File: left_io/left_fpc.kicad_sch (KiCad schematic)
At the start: 1 part

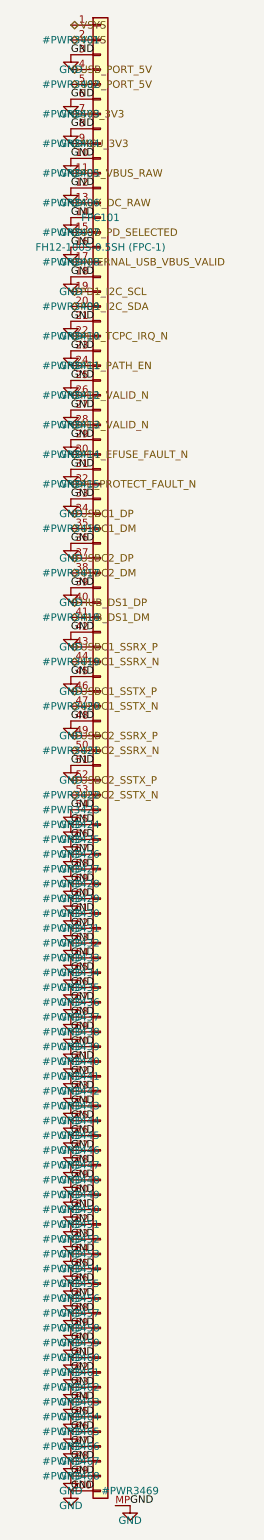
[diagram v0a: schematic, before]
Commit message: Phase 4 deep audit: FH41-68S connectors, placement hygiene, one-shot fixes
Found and fixed four board-killers in the pre-fab audit:

1. Fictional connector: the Hirose FH12 series stops at 60 positions, so
   the 100-pin FH12-100S used for FPC-1/FPC-2 does not exist.  Replaced
   with the FH41-68S-0.5SH(05) (shielded-FFC, 68 positions; FPC-1 uses
   pins 1-53, FPC-2 pins 1-61):
   - new footprint derived from KiCad's FH41-30S (68 signal pads, MP at
     +/-18, 14 SH solder-holds, 38mm body) with SH pads tied to GND
   - new 68-pin symbol (Conn_01x68_FFC_MP), pin maps trimmed to 68
   - fictional FH12-100S footprint/symbol/script removed
   - cable spec updated (68-pin shielded FFC, one type for both)

2. Connector courtyard conflicts: parts sat under connector bodies
   (pads cleared, bodies collided).  Placement now enforces courtyard
   clearance against the connector body; the resolver scans with
   courtyard checks; a double-shift bug that hid re-placed parts' true
   positions was fixed.

3. FPC-3 orientation: the FH12's FPC enters from the +y side; both FPC-3
   connectors faced away from the seam.  FPC105 -> (123.5, 6.5) rot 180,
   FPC106 -> (30, 54) rot 0 so the cable exits the center bottom edge
   and enters the BMS top edge.

4. Original-layout defects: 16 genuine pad-pad shorts (inductor pads
   swallowing caps, passives on each other, parts on mounting holes) and
   23 parts inside the hinge cutouts (physically off the board) are all
   moved to legal spots; zones refilled against the final placement.

New post-build hygiene sweep (fix_board_hygiene.py) uses the final board
text as the geometry oracle, converges to a clean state, and reports
residuals instead of dropping them.

Final DRC: 0 shorts / 0 clearance / 0 hole violations on all four boards
(bms fully clean).  Remaining: courtyard touches around the Mu socket and
M.2 slot (design-inherent moat), chassis-edge copper, zone islands, silk
cosmetics, and unrouted nets (Phase 4b).  Gate: SCHEMATIC R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
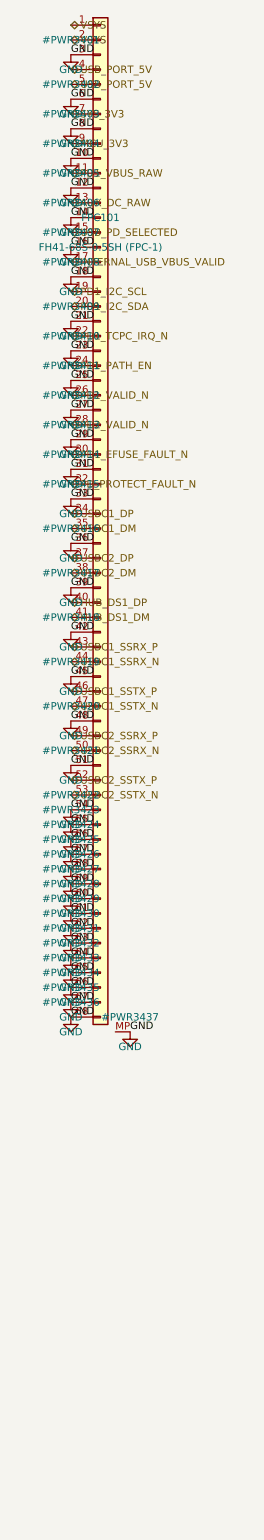
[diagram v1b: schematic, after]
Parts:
- FPC101: value FH12-100S-0.5SH (FPC-1) -> FH41-68S-0.5SH (FPC-1); footprint ducktop2:FH12-100S-0.5SH_1x100-1MP_P0.50mm_Horizontal -> ducktop2:Hirose_FH41-68S-0.5SH_1x68_1MP_1SH_P0.5mm_Horizontal; symbol Conn_01x100_FFC_MP:Conn_01x100_FFC_MP -> Conn_01x68_FFC_MP:Conn_01x68_FFC_MP
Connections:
- net GND: no longer FPC101.100 (Pin_100), FPC101.69 (Pin_69), FPC101.70 (Pin_70), FPC101.71 (Pin_71), FPC101.72 (Pin_72), FPC101.73 (Pin_73), FPC101.74 (Pin_74), FPC101.75 (Pin_75), FPC101.76 (Pin_76), FPC101.77 (Pin_77), FPC101.78 (Pin_78), FPC101.79 (Pin_79), FPC101.80 (Pin_80), FPC101.81 (Pin_81), FPC101.82 (Pin_82), FPC101.83 (Pin_83), FPC101.84 (Pin_84), FPC101.85 (Pin_85), FPC101.86 (Pin_86), FPC101.87 (Pin_87), FPC101.88 (Pin_88), FPC101.89 (Pin_89), FPC101.90 (Pin_90), FPC101.91 (Pin_91), FPC101.92 (Pin_92), FPC101.93 (Pin_93), FPC101.94 (Pin_94), FPC101.95 (Pin_95), FPC101.96 (Pin_96), FPC101.97 (Pin_97), FPC101.98 (Pin_98), FPC101.99 (Pin_99)

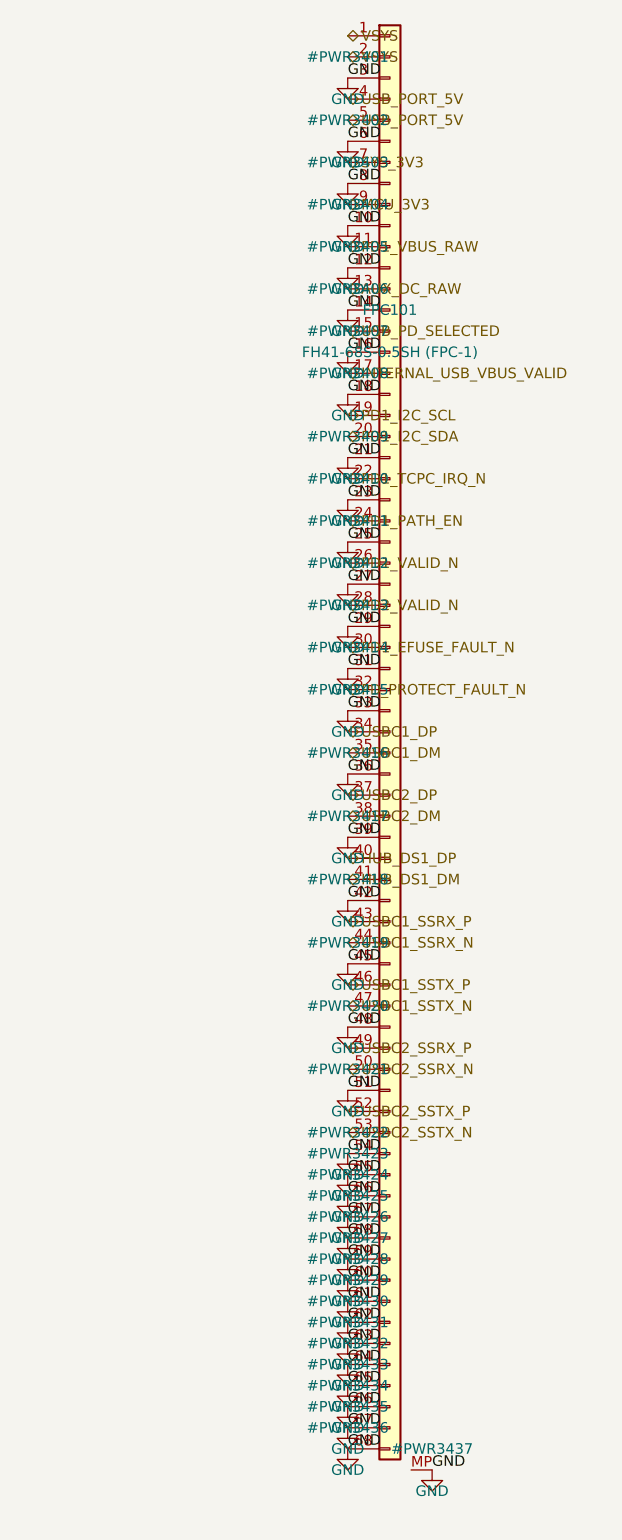
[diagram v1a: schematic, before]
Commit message: Phase 5: second-opinion audit remediation + rebuilt, verified board pipeline
Second-opinion AI audit found A-tier defects; remediation applied and the
board pipeline rebuilt on a known-good base with the fixes it needed:

- electrical: LTC4418IUF symbol pinout corrected (both selectors were
  dead as drawn); center charge cascade (U15 <- U15B, PD1 > PD2 > AUX);
  pack negative never crosses FPC-3, 15-pin FG_VSS return; power-budgeted
  FPC pin maps (0.4 A/pin derate); J12/DS4 completed; AUX source fuse
- FH41-68S footprint: 13 datasheet-correct SH pads + SH pin in symbol
- connector geometry settled against the Hirose FH12 2D drawing: FFC
  enters opposite the solder pins (mouth = local +Y); reversed side-B
  maps are correct for the 180-deg-mounted pairs; rotations set so mouths
  face across every seam
- pipeline (generate_split_boards.py): per-pin pad-net resync from the
  netlists (kills shadow nets for good), netlist-exact name
  normalization, netlist-only part injection (cascade, probe headers),
  zone refill after outline swap, read-before-write race fixed, orphan
  parts dropped loudly, non-zero exit on unresolved overlaps
- monolith board relocated to old/monolith_ducktop2.kicad_pcb (placement
  oracle for the center cut only)

verified end state: 4 boards 0 shorts / 0 clearance / 0 drill, 0 boundary
crossings, 6/6 connectors contract-exact with mouths facing, 0 shadow
nets, gates PASS x4, ERC 0 x4. routing next (499 nets/board).
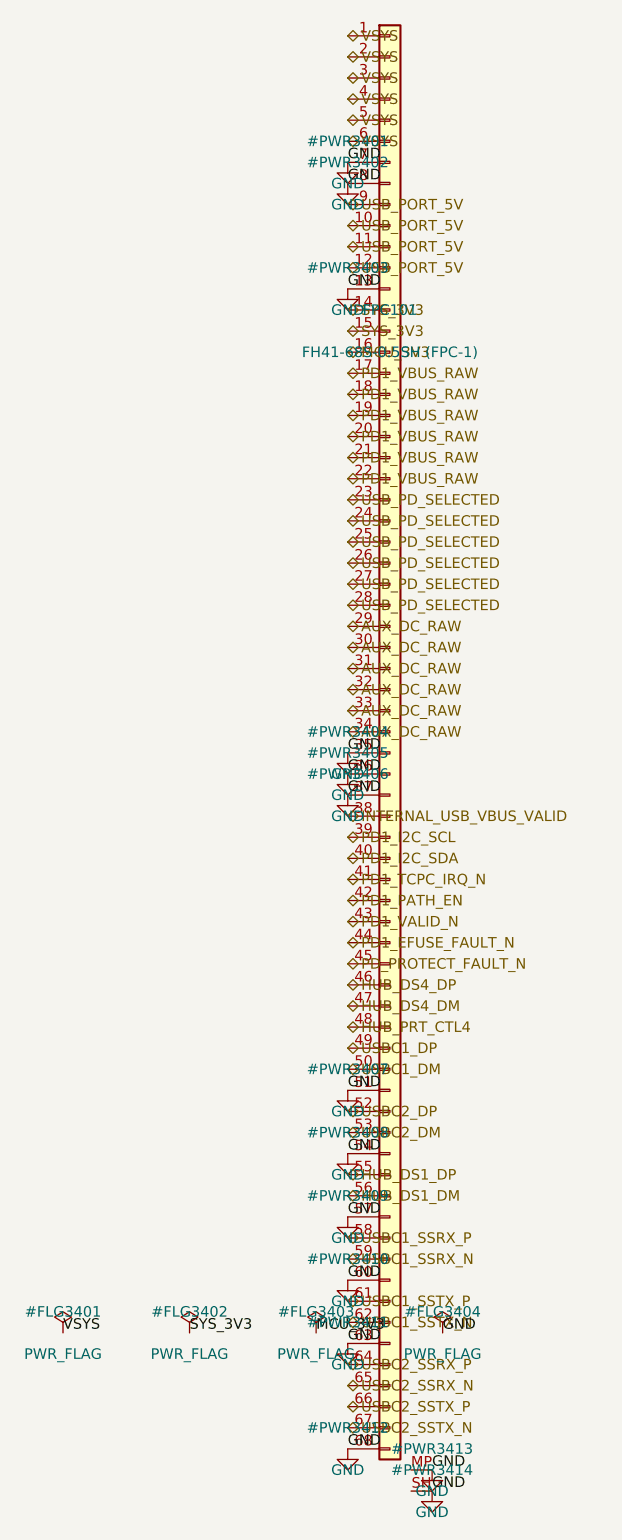
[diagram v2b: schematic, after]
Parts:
- FPC101: MPN (none) -> FH41-68S-0.5SH(05); Manufacturer (none) -> Hirose
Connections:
- net PD2_VALID_N is gone; now on net USB_PD_SELECTED: FPC101.28 (Pin_28)
- net AUX_DC_RAW: now also FPC101.29 (Pin_29), FPC101.30 (Pin_30), FPC101.31 (Pin_31), FPC101.32 (Pin_32), FPC101.33 (Pin_33), FPC101.34 (Pin_34); no longer FPC101.13 (Pin_13)
- net GND: now also FPC101.13 (Pin_13), FPC101.35 (Pin_35), FPC101.37 (Pin_37), FPC101.7 (Pin_7), FPC101.SH; no longer FPC101.10 (Pin_10), FPC101.12 (Pin_12), FPC101.14 (Pin_14), FPC101.16 (Pin_16), FPC101.18 (Pin_18), FPC101.21 (Pin_21), FPC101.23 (Pin_23), FPC101.25 (Pin_25), FPC101.27 (Pin_27), FPC101.29 (Pin_29), FPC101.3 (Pin_3), FPC101.31 (Pin_31), FPC101.33 (Pin_33), FPC101.39 (Pin_39), FPC101.42 (Pin_42), FPC101.45 (Pin_45), FPC101.48 (Pin_48), FPC101.55 (Pin_55), FPC101.56 (Pin_56), FPC101.58 (Pin_58), FPC101.59 (Pin_59), FPC101.6 (Pin_6), FPC101.61 (Pin_61), FPC101.62 (Pin_62), FPC101.64 (Pin_64), FPC101.65 (Pin_65), FPC101.66 (Pin_66), FPC101.67 (Pin_67)
- net HUB_DS1_DM: now also FPC101.56 (Pin_56); no longer FPC101.41 (Pin_41)
- net HUB_DS1_DP: now also FPC101.55 (Pin_55); no longer FPC101.40 (Pin_40)
- net INTERNAL_USB_VBUS_VALID: now also FPC101.38 (Pin_38); no longer FPC101.17 (Pin_17)
- net MCU_3V3: now also FPC101.16 (Pin_16); no longer FPC101.9 (Pin_9)
- net PD1_EFUSE_FAULT_N: now also FPC101.44 (Pin_44); no longer FPC101.30 (Pin_30)
- net PD1_I2C_SCL: now also FPC101.39 (Pin_39); no longer FPC101.19 (Pin_19)
- net PD1_I2C_SDA: now also FPC101.40 (Pin_40); no longer FPC101.20 (Pin_20)
- net PD1_PATH_EN: now also FPC101.42 (Pin_42); no longer FPC101.24 (Pin_24)
- net PD1_TCPC_IRQ_N: now also FPC101.41 (Pin_41); no longer FPC101.22 (Pin_22)
- net PD1_VALID_N: now also FPC101.43 (Pin_43); no longer FPC101.26 (Pin_26)
- net PD1_VBUS_RAW: now also FPC101.17 (Pin_17), FPC101.18 (Pin_18), FPC101.19 (Pin_19), FPC101.20 (Pin_20), FPC101.21 (Pin_21), FPC101.22 (Pin_22); no longer FPC101.11 (Pin_11)
- net PD_PROTECT_FAULT_N: now also FPC101.45 (Pin_45); no longer FPC101.32 (Pin_32)
- net SYS_3V3: now also FPC101.14 (Pin_14), FPC101.15 (Pin_15); no longer FPC101.7 (Pin_7)
- net USBC1_DM: now also FPC101.50 (Pin_50); no longer FPC101.35 (Pin_35)
- net USBC1_DP: now also FPC101.49 (Pin_49); no longer FPC101.34 (Pin_34)
- net USBC1_SSRX_N: now also FPC101.59 (Pin_59); no longer FPC101.44 (Pin_44)
- net USBC1_SSRX_P: now also FPC101.58 (Pin_58); no longer FPC101.43 (Pin_43)
- net USBC1_SSTX_N: now also FPC101.62 (Pin_62); no longer FPC101.47 (Pin_47)
- net USBC1_SSTX_P: now also FPC101.61 (Pin_61); no longer FPC101.46 (Pin_46)
- net USBC2_DM: now also FPC101.53 (Pin_53); no longer FPC101.38 (Pin_38)
- net USBC2_DP: now also FPC101.52 (Pin_52); no longer FPC101.37 (Pin_37)
- net USBC2_SSRX_N: now also FPC101.65 (Pin_65); no longer FPC101.50 (Pin_50)
- net USBC2_SSRX_P: now also FPC101.64 (Pin_64); no longer FPC101.49 (Pin_49)
- net USBC2_SSTX_N: now also FPC101.67 (Pin_67); no longer FPC101.53 (Pin_53)
- net USBC2_SSTX_P: now also FPC101.66 (Pin_66); no longer FPC101.52 (Pin_52)
- net USB_PD_SELECTED: now also FPC101.23 (Pin_23), FPC101.24 (Pin_24), FPC101.25 (Pin_25), FPC101.26 (Pin_26), FPC101.27 (Pin_27); no longer FPC101.15 (Pin_15)
- net USB_PORT_5V: now also FPC101.10 (Pin_10), FPC101.11 (Pin_11), FPC101.12 (Pin_12), FPC101.9 (Pin_9); no longer FPC101.4 (Pin_4), FPC101.5 (Pin_5)
- net VSYS: now also FPC101.3 (Pin_3), FPC101.4 (Pin_4), FPC101.5 (Pin_5), FPC101.6 (Pin_6)
- new net HUB_DS4_DM: FPC101.47 (Pin_47)
- new net HUB_DS4_DP: FPC101.46 (Pin_46)
- new net HUB_PRT_CTL4: FPC101.48 (Pin_48)

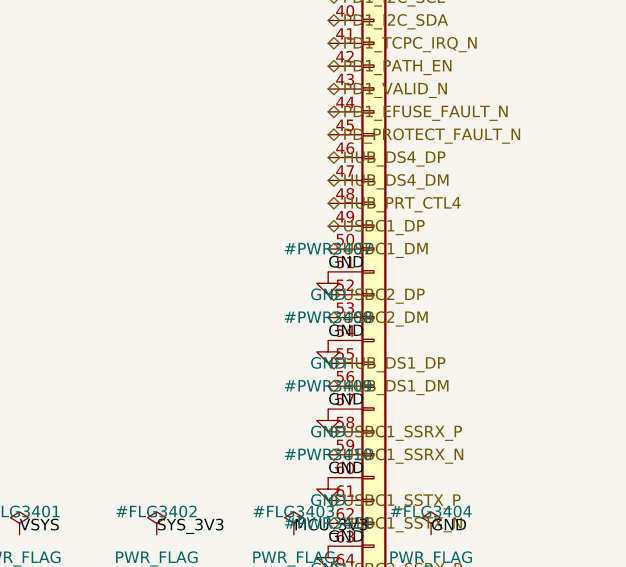
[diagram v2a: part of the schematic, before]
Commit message: get the main boards ready for routing
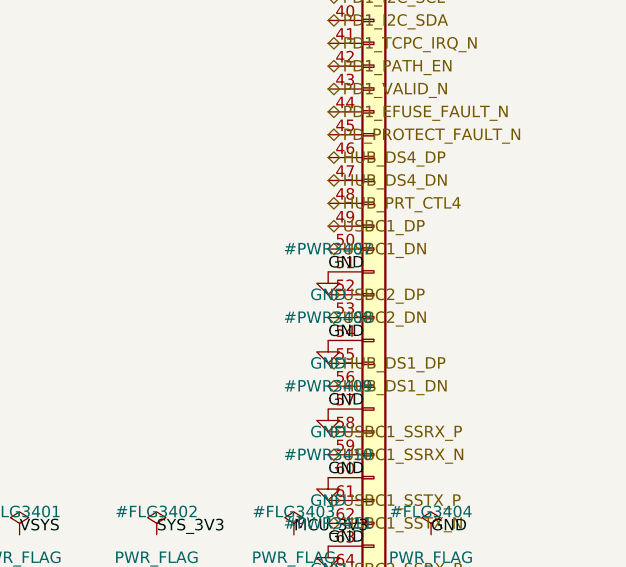
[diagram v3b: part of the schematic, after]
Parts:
- FPC101: MPN FH41-68S-0.5SH(05) -> FH41-68S-0.5SH(28)
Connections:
- net HUB_DS1_DM renamed HUB_DS1_DN
- net HUB_DS4_DM renamed HUB_DS4_DN
- net USBC1_DM renamed USBC1_DN
- net USBC2_DM renamed USBC2_DN
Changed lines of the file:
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@@
   (property "Datasheet" "" (at 59.69 299.72 0) (effects (font (size 1.27 1.27)) (hide yes)))
   (property "Manufacturer" "Hirose" (at 59.69 299.72 0) (effects (font (size 1.27 1.27)) (hide yes)))
-  (property "MPN" "FH41-68S-0.5SH(05)" (at 59.69 299.72 0) (effects (font (size 1.27 1.27)) (hide yes)))
+  (property "MPN" "FH41-68S-0.5SH(28)" (at 59.69 299.72 0) (effects (font (size 1.27 1.27)) (hide yes)))
   (pin "1")
   (pin "2")
@@
   (effects (font (size 1.27 1.27)) (justify left bottom))
 )
-(hierarchical_label "HUB_DS4_DM"
+(hierarchical_label "HUB_DS4_DN"
   (shape bidirectional)
   (at 54.61 381 0)
@@
   (effects (font (size 1.27 1.27)) (justify left bottom))
 )
-(hierarchical_label "USBC1_DM"
+(hierarchical_label "USBC1_DN"
   (shape bidirectional)
   (at 54.61 388.62 0)
@@
   (effects (font (size 1.27 1.27)) (justify left bottom))
 )
-(hierarchical_label "USBC2_DM"
+(hierarchical_label "USBC2_DN"
   (shape bidirectional)
   (at 54.61 396.24 0)
@@
   (effects (font (size 1.27 1.27)) (justify left bottom))
 )
-(hierarchical_label "HUB_DS1_DM"
+(hierarchical_label "HUB_DS1_DN"
   (shape bidirectional)
   (at 54.61 403.86 0)

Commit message: fix more power stuff and update the left board
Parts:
- added J2431: left power loom, straight-numbered, Connector_Molex:Molex_Micro-Fit_3.0_43045-1212_2x06_P3.00mm_Vertical, symbol Connector_Generic:Conn_02x06_Odd_Even
- added J2434: USB5 direct power loom, ducktop2:AMASS_XT30PW-F30_G_Y, symbol Connector_Generic:Conn_01x02
- added J2440, J2442: main ground strap, Connector_Wire:SolderWirePad_1x01_SMD_5x10mm, symbol Connector:TestPoint
- added R2440, R2441: 0.33, Resistor_SMD:R_0603_1608Metric, symbol Device:R
- FPC101: value FH41-68S-0.5SH (FPC-1) -> Molex5039084120 signal cable; footprint ducktop2:Hirose_FH41-68S-0.5SH_1x68_1MP_1SH_P0.5mm_Horizontal -> ducktop2:Molex_5039084120_1x41_P0.50mm_Horizontal; symbol Conn_01x68_FFC_MP:Conn_01x68_FFC_MP -> Conn_01x41_Signal_SH:Conn_01x41_Signal_SH; MPN FH41-68S-0.5SH(28) -> 5039084120; Manufacturer Hirose -> Molex
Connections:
- net AUX_DC_RAW: now also J2431.4 (Pin_4); no longer FPC101.29 (Pin_29), FPC101.30 (Pin_30), FPC101.31 (Pin_31), FPC101.32 (Pin_32), FPC101.33 (Pin_33), FPC101.34 (Pin_34)
- net GND: now also FPC101.1, FPC101.10, FPC101.16, FPC101.19, FPC101.22, FPC101.25, FPC101.29, FPC101.33, FPC101.4, J2431.10 (Pin_10), J2431.11 (Pin_11), J2431.12 (Pin_12), J2431.7 (Pin_7), J2431.8 (Pin_8), J2431.9 (Pin_9), J2434.1 (Pin_1), J2440.1, J2442.1, R2440.2, R2441.2; no longer FPC101.35 (Pin_35), FPC101.36 (Pin_36), FPC101.51 (Pin_51), FPC101.54 (Pin_54), FPC101.57 (Pin_57), FPC101.60 (Pin_60), FPC101.63 (Pin_63), FPC101.68 (Pin_68), FPC101.8 (Pin_8), FPC101.MP, FPC101.SH
- net HUB_DS1_DN: now also FPC101.21; no longer FPC101.56 (Pin_56)
- net HUB_DS1_DP: now also FPC101.20; no longer FPC101.55 (Pin_55)
- net HUB_DS4_DN: now also FPC101.24; no longer FPC101.47 (Pin_47)
- net HUB_DS4_DP: now also FPC101.23; no longer FPC101.46 (Pin_46)
- net HUB_PRT_CTL4: now also FPC101.40; no longer FPC101.48 (Pin_48)
- net INTERNAL_USB_VBUS_VALID: now also FPC101.41; no longer FPC101.38 (Pin_38)
- net MCU_3V3: now also J2431.6 (Pin_6); no longer FPC101.16 (Pin_16)
- net PD1_EFUSE_FAULT_N: now also FPC101.32; no longer FPC101.44 (Pin_44)
- net PD1_I2C_SCL: now also FPC101.26; no longer FPC101.39 (Pin_39)
- net PD1_I2C_SDA: now also FPC101.27; no longer FPC101.40 (Pin_40)
- net PD1_PATH_EN: now also FPC101.30; no longer FPC101.42 (Pin_42)
- net PD1_TCPC_IRQ_N: now also FPC101.28; no longer FPC101.41 (Pin_41)
- net PD1_VALID_N: now also FPC101.31; no longer FPC101.43 (Pin_43)
- net PD1_VBUS_RAW: now also J2431.2 (Pin_2); no longer FPC101.17 (Pin_17), FPC101.18 (Pin_18), FPC101.19 (Pin_19), FPC101.20 (Pin_20), FPC101.21 (Pin_21), FPC101.22 (Pin_22)
- net PD_PROTECT_FAULT_N: now also FPC101.34; no longer FPC101.45 (Pin_45)
- net SYS_3V3: now also J2431.5 (Pin_5); no longer FPC101.14 (Pin_14), FPC101.15 (Pin_15)
- net USBC1_DN: now also FPC101.15; no longer FPC101.50 (Pin_50)
- net USBC1_DP: now also FPC101.14; no longer FPC101.49 (Pin_49)
- net USBC1_SSRX_N: now also FPC101.3; no longer FPC101.59 (Pin_59)
- net USBC1_SSRX_P: now also FPC101.2; no longer FPC101.58 (Pin_58)
- net USBC1_SSTX_N: now also FPC101.6; no longer FPC101.62 (Pin_62)
- net USBC1_SSTX_P: now also FPC101.5; no longer FPC101.61 (Pin_61)
- net USBC2_DN: now also FPC101.18; no longer FPC101.53 (Pin_53)
- net USBC2_DP: now also FPC101.17; no longer FPC101.52 (Pin_52)
- net USBC2_SSRX_N: now also FPC101.9; no longer FPC101.65 (Pin_65)
- net USBC2_SSRX_P: now also FPC101.8; no longer FPC101.64 (Pin_64)
- net USBC2_SSTX_N: now also FPC101.12; no longer FPC101.67 (Pin_67)
- net USBC2_SSTX_P: now also FPC101.11; no longer FPC101.66 (Pin_66)
- net USB_PD_SELECTED: now also J2431.3 (Pin_3); no longer FPC101.23 (Pin_23), FPC101.24 (Pin_24), FPC101.25 (Pin_25), FPC101.26 (Pin_26), FPC101.27 (Pin_27), FPC101.28 (Pin_28)
- net USB_PORT_5V: now also J2434.2 (Pin_2); no longer FPC101.10 (Pin_10), FPC101.11 (Pin_11), FPC101.12 (Pin_12), FPC101.9 (Pin_9)
- net VSYS: now also J2431.1 (Pin_1); no longer FPC101.1 (Pin_1), FPC101.2 (Pin_2), FPC101.3 (Pin_3), FPC101.4 (Pin_4), FPC101.5 (Pin_5), FPC101.6 (Pin_6)
- new net FPC101_SHELL: FPC101.SH, R2440.1, R2441.1
- new net PD2_SOURCE_PG: FPC101.36
- new net SERVICE_MUX_RESET_N: FPC101.35
- new net USB_J11_PERMIT: FPC101.38
- new net USB_J12_PERMIT: FPC101.39
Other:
- note added: "Both ground straps must be fitted before the signal cable. Keep raw and protected battery returns separate from these main-board grounds."
- note added: "Power uses the separate rated looms. The signal cable carries no positive supply rails."
- note added: "The shell uses two parallel 0.33 ohm returns at each connector. Numbered ground conductors connect directly to the local ground plane."

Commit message: fix the center layout and more board issues
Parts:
- J2434: CableEnvelope rounded exit path 370.47 mm GND / 380.47 mm USB5; retain up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 -> rounded exit path 354.47 mm GND / 364.47 mm USB5; retain up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
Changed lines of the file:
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@@
   (property "ResistanceAcceptance" "each mated/soldered termination <=5 mOhm hot/aged; wire <=30 mOhm/m hot" (at 229.87 229.87 0) (effects (font (size 1.27 1.27)) (hide yes)))
   (property "MatedEnvelope" "23.10 x 13.60 x 5.75 mm conservative; reserve sleeve and 18.80 mm wire bend radius" (at 229.87 229.87 0) (effects (font (size 1.27 1.27)) (hide yes)))
-  (property "CableEnvelope" "rounded exit path 370.47 mm GND / 380.47 mm USB5; retain up to 12 mm termination/sleeve allowance and fit remaining height/service detour before assembly" (at 229.87 229.87 0) (effects (font (size 1.27 1.27)) (hide yes)))
+  (property "CableEnvelope" "rounded exit path 354.47 mm GND / 364.47 mm USB5; retain up to 12 mm termination/sleeve allowance and fit remaining height/service detour before assembly" (at 229.87 229.87 0) (effects (font (size 1.27 1.27)) (hide yes)))
   (property "Assembly" "unpowered mating only; insulate solder joints and strain-relieve wires independently; retention lands isolated" (at 229.87 229.87 0) (effects (font (size 1.27 1.27)) (hide yes)))
   (property "Fabrication" "power holes 1.85 +/-0.05 mm, retention holes 1.15 +/-0.05 mm finished diameter" (at 229.87 229.87 0) (effects (font (size 1.27 1.27)) (hide yes)))
